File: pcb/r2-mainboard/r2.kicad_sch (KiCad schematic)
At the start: 0 parts

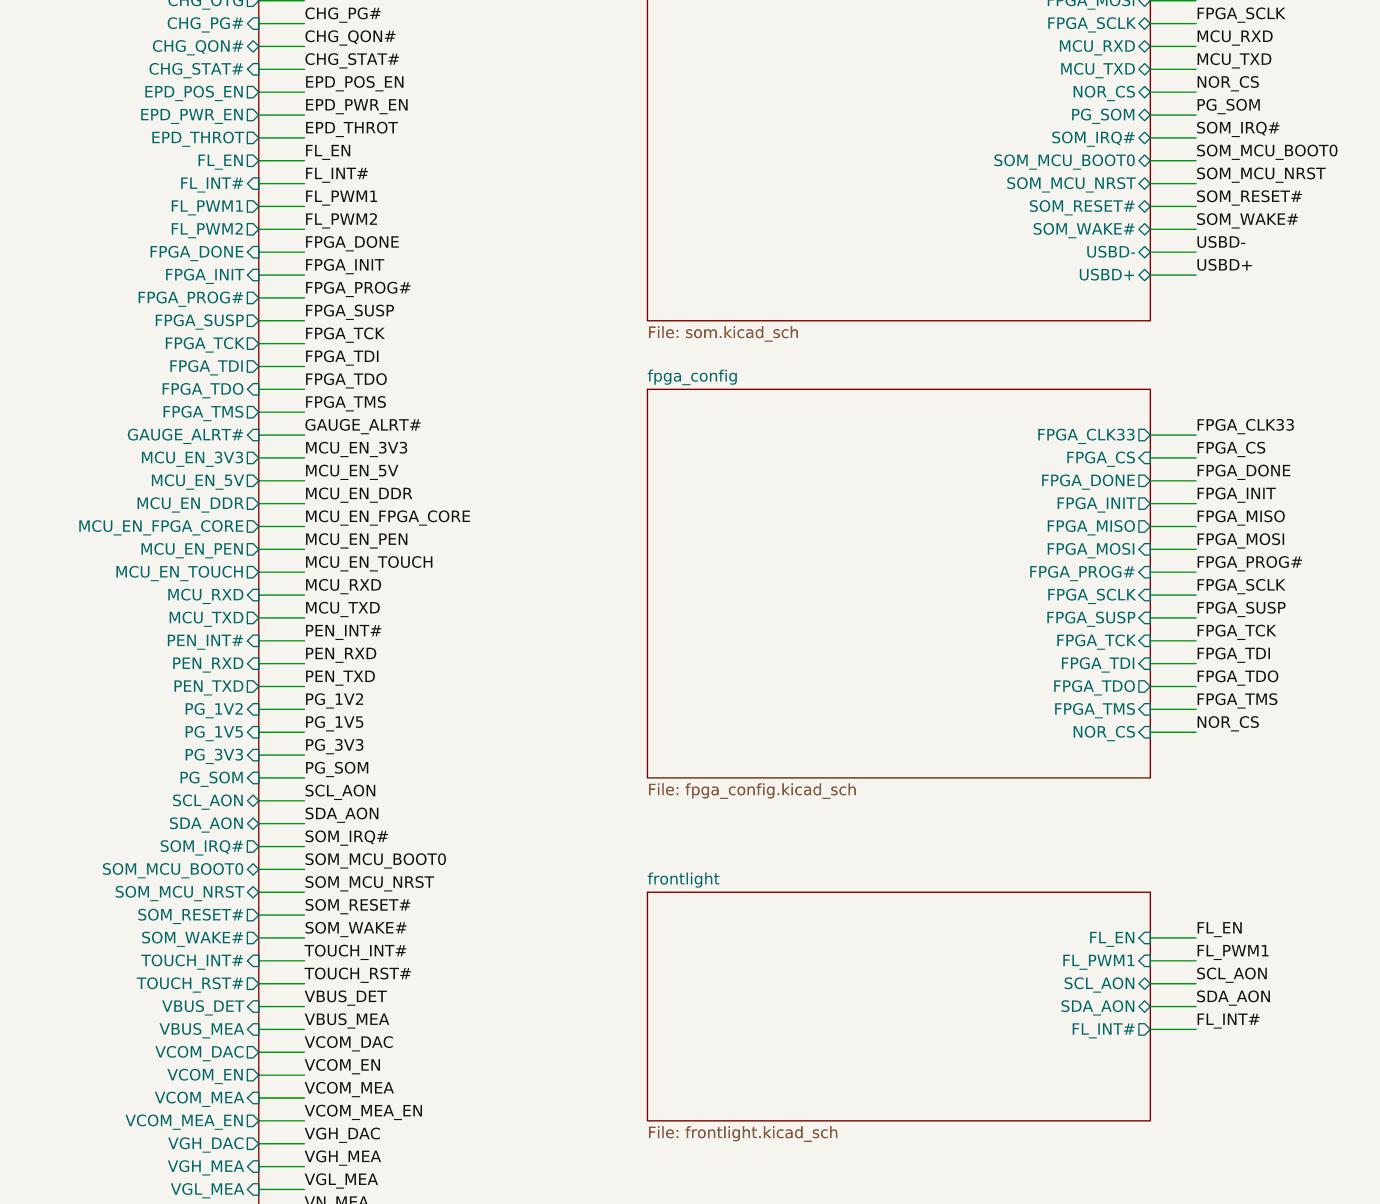
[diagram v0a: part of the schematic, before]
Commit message: routing and board layout
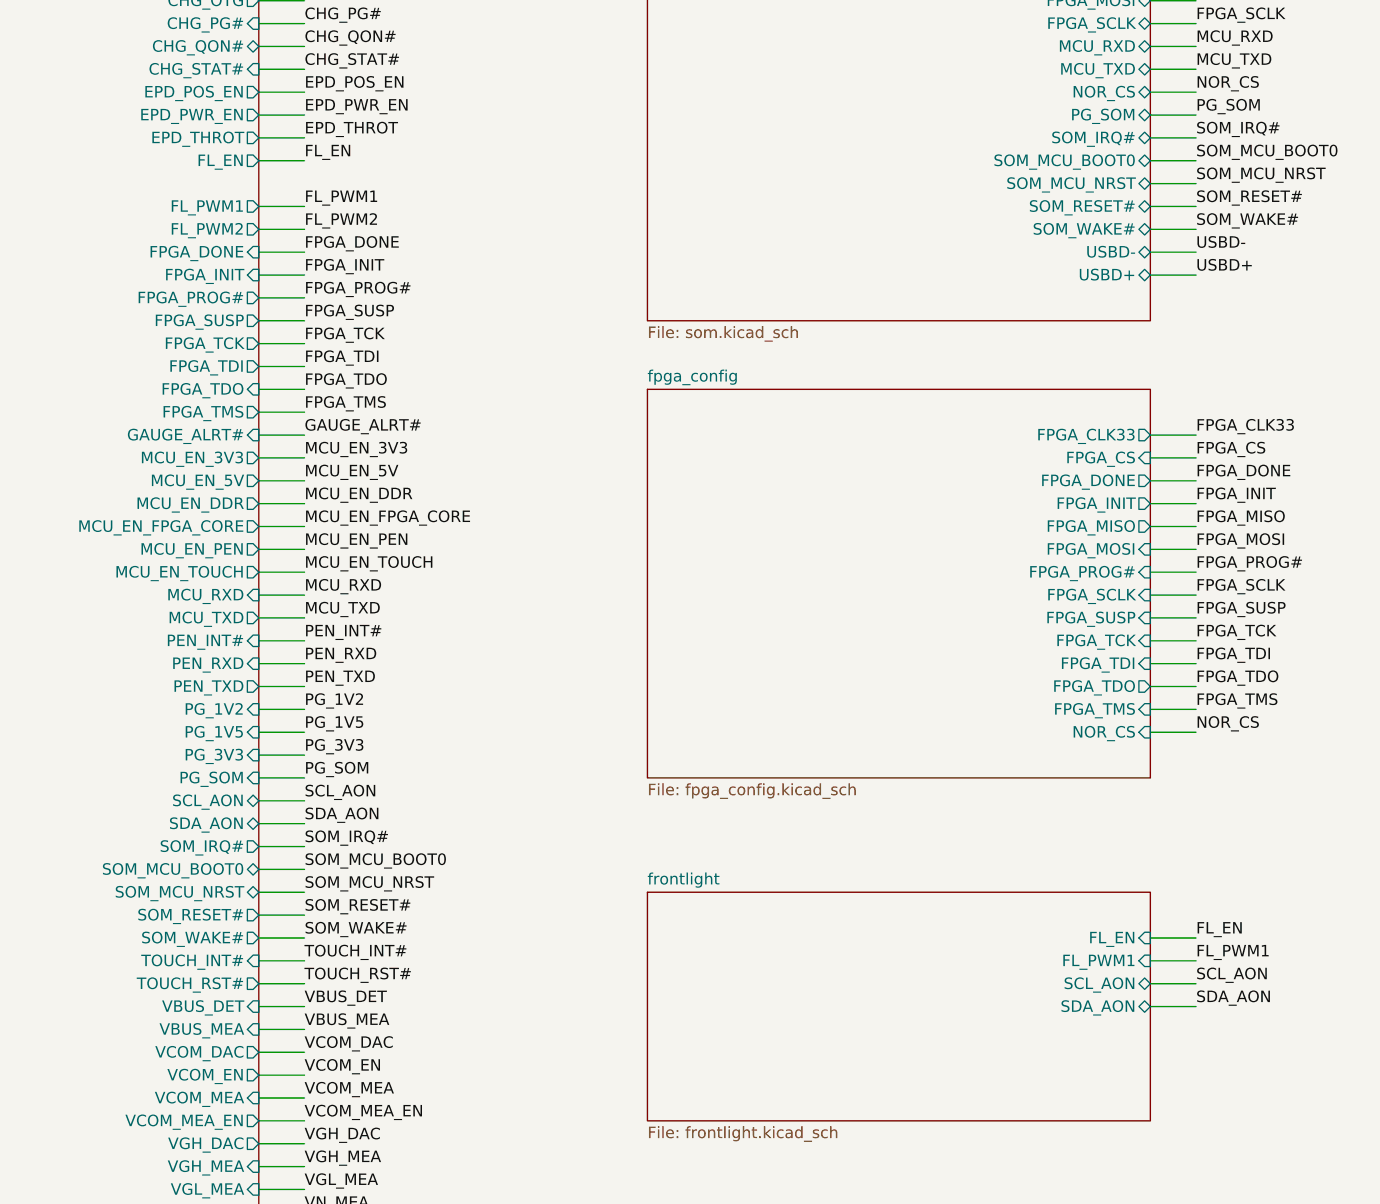
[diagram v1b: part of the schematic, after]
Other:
- sheet frontlight ports: added none; removed FL_INT#
- sheet mcu ports: added none; removed FL_INT#
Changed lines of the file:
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@@
 	(wire
 		(pts
-			(xy 276.86 60.96) (xy 281.94 60.96)
-		)
-		(stroke
-			(width 0)
-			(type default)
-		)
-	)
-	(wire
-		(pts
 			(xy 177.8 111.76) (xy 182.88 111.76)
 		)
@@
 	(wire
 		(pts
-			(xy 375.92 154.94) (xy 381 154.94)
-		)
-		(stroke
-			(width 0)
-			(type default)
-		)
-	)
-	(wire
-		(pts
 			(xy 78.74 284.48) (xy 83.82 284.48)
 		)
@@
 		)
 	)
-	(label "FL_INT#"
-		(at 381 154.94 0)
-		(effects
-			(font
-				(size 1.27 1.27)
-			)
-			(justify left bottom)
-		)
-	)
 	(label "DPI_R5"
 		(at 182.88 119.38 0)
@@
 		)
 	)
-	(label "FL_INT#"
-		(at 281.94 60.96 0)
-		(effects
-			(font
-				(size 1.27 1.27)
-			)
-			(justify left bottom)
-		)
-	)
 	(label "SDA_AON"
 		(at 83.82 289.56 0)
@@
 			)
 		)
-		(pin "FL_INT#" output
-			(at 375.92 154.94 0)
-			(effects
-				(font
-					(size 1.27 1.27)
-				)
-				(justify right)
-			)
-		)
 		(instances
 			(project "r2"
@@
 			(effects
 				(font
-					(size 1.27 1.27)
-				)
-				(justify right)
-			)
-		)
-		(pin "FL_INT#" input
-			(at 276.86 60.96 0)
-			(effects
-				(font
